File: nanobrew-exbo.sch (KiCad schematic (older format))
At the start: 12 parts, among them J1 RPi_GPIO, J2 DS18B20 sensors, J3 driver_terminal, J4 driver_terminal, J5 PWR IN 1, J6 PI POWER, J7 PWR IN 2, J8 adc_terminal, U1 ULN2803A, U2 ULN2803A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

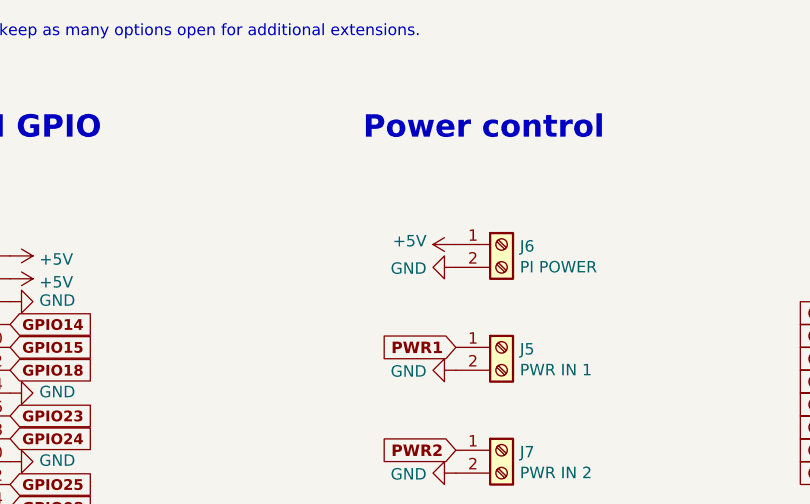
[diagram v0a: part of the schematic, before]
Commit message: Adding capacitor
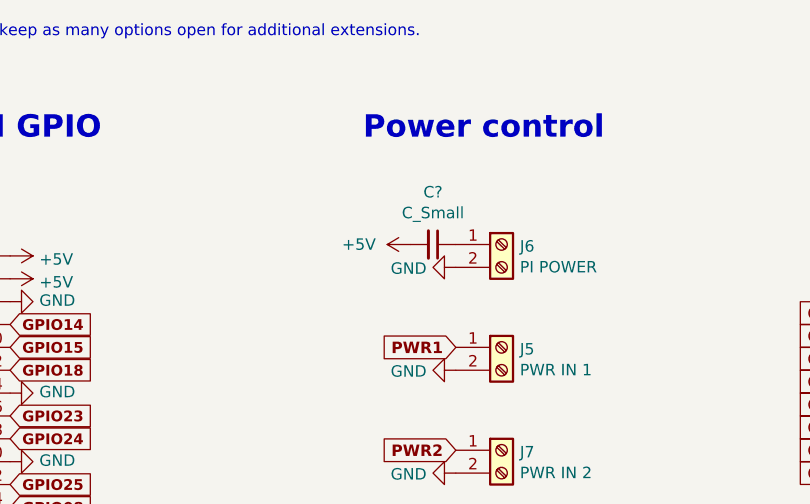
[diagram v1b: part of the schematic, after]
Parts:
- added C?: C_Small, Capacitor_THT:CP_Radial_D4.0mm_P2.00mm, symbol Device:C_Small
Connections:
- net +5V: now also C?.2; no longer J6.1 (Pin_1)
- new net: C?.1, J6.1 (Pin_1)
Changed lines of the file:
@@
 L power:+5V #PWR0112
 U 1 1 5FA61E6C
-P 4450 1550
-F 0 "#PWR0112" H 4450 1400 50  0001 C CNN
-F 1 "+5V" V 4465 1678 50  0000 L CNN
-F 2 "" H 4450 1550 50  0001 C CNN
-F 3 "" H 4450 1550 50  0001 C CNN
-	1    4450 1550
+P 4250 1550
+F 0 "#PWR0112" H 4250 1400 50  0001 C CNN
+F 1 "+5V" V 4250 1700 50  0000 L CNN
+F 2 "" H 4250 1550 50  0001 C CNN
+F 3 "" H 4250 1550 50  0001 C CNN
+	1    4250 1550
 	0    -1   -1   0
 $EndComp
@@
 Wire Wire Line
 	2300 5500 2200 5500
+$Comp
+L Device:C_Small C?
+U 1 1 5FDBC239
+P 4350 1550
+F 0 "C?" V 4121 1550 50  0000 C CNN
+F 1 "C_Small" V 4212 1550 50  0000 C CNN
+F 2 "Capacitor_THT:CP_Radial_D4.0mm_P2.00mm" H 4350 1550 50  0001 C CNN
+F 3 "~" H 4350 1550 50  0001 C CNN
+	1    4350 1550
+	0    1    1    0
+$EndComp
 $EndSCHEMATC

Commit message: Removing old files.
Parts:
- gave numbers to parts that had none: 1
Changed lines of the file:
@@
 	2250 5350 2600 5350
 $Comp
-L power:+5V #PWR?
+L power:+5V #PWR0113
 U 1 1 5FBBF92D
 P 3150 5450
-F 0 "#PWR?" H 3150 5300 50  0001 C CNN
+F 0 "#PWR0113" H 3150 5300 50  0001 C CNN
 F 1 "+5V" V 3165 5578 50  0000 L CNN
 F 2 "" H 3150 5450 50  0001 C CNN
@@
 	2300 5500 2200 5500
 $Comp
-L Device:C_Small C?
+L Device:C_Small C1
 U 1 1 5FDBC239
 P 4350 1550
-F 0 "C?" V 4121 1550 50  0000 C CNN
+F 0 "C1" V 4121 1550 50  0000 C CNN
 F 1 "C_Small" V 4212 1550 50  0000 C CNN
 F 2 "Capacitor_THT:CP_Radial_D4.0mm_P2.00mm" H 4350 1550 50  0001 C CNN
